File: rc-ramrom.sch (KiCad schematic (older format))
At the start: 23 parts, among them J1 RC2014, U1 EPROM, U2 AS6C1008, U3 74HCT4075, U4 74HCT74, U5 74HCT138

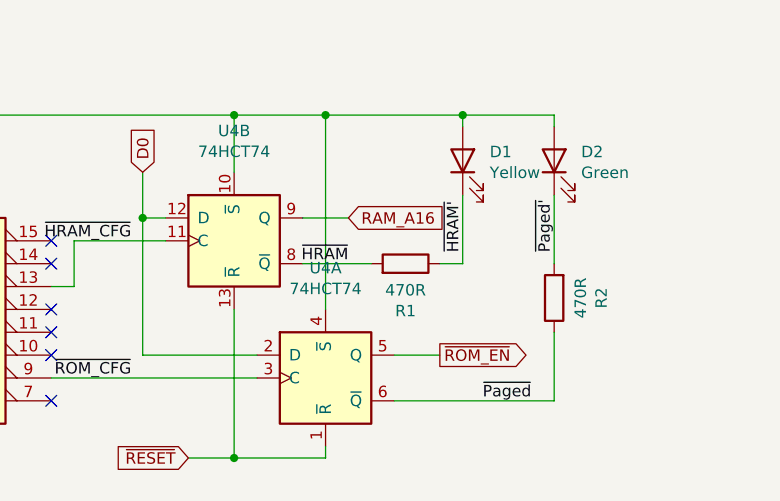
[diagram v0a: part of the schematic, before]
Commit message: Neatened routing
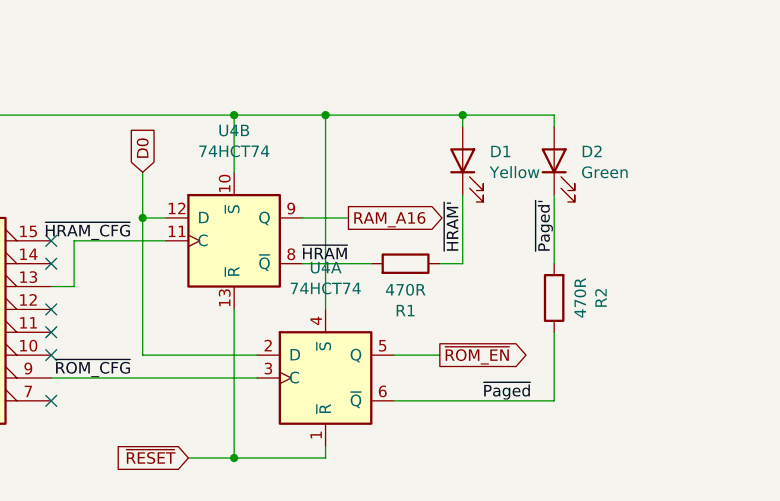
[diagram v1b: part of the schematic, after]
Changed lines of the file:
@@
 Wire Wire Line
 	3000 6400 2800 6400
-Text GLabel 9100 1650 2    50   Input ~ 0
+Text GLabel 9100 1650 2    50   Output ~ 0
 RAM_A16
 Wire Wire Line

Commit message: Updated silk, moved to v1.0
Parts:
- D1: value Yellow -> Green
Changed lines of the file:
@@
 P 9600 1400
 F 0 "D1" V 9639 1282 50  0000 R CNN
-F 1 "Yellow" V 9548 1282 50  0000 R CNN
+F 1 "Green" V 9548 1282 50  0000 R CNN
 F 2 "LED_THT:LED_D3.0mm" H 9600 1400 50  0001 C CNN
 F 3 "~" H 9600 1400 50  0001 C CNN
